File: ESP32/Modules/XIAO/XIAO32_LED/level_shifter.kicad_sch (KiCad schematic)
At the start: 1 part, among them U3 74AHCT125

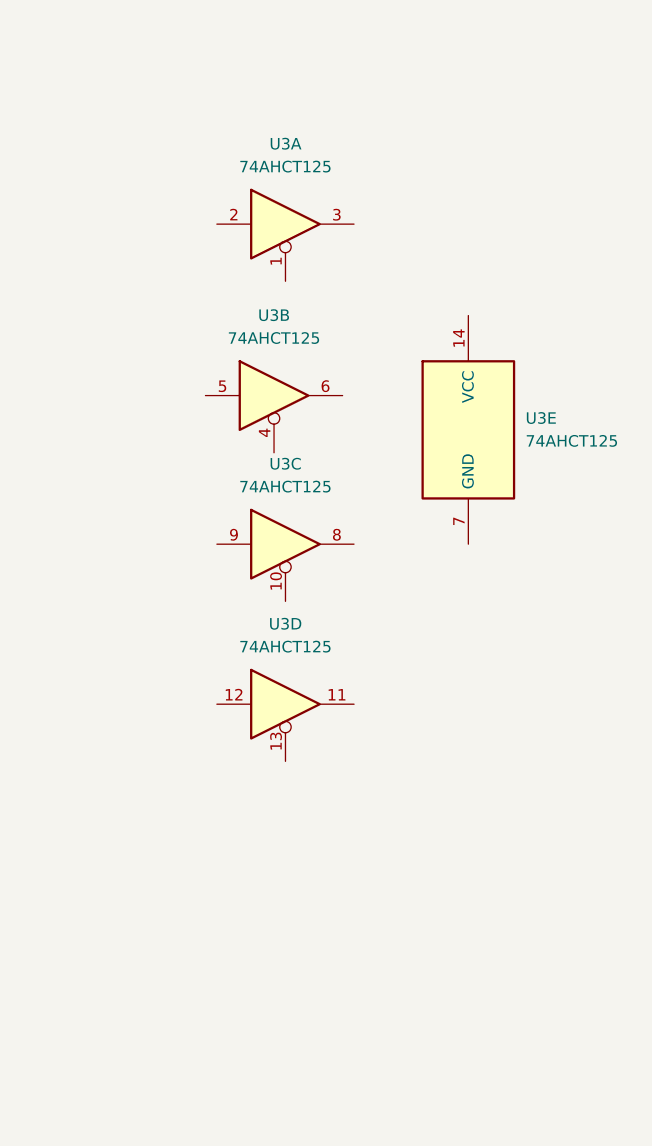
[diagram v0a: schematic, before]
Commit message: XIAO32_LED: MCU wired up
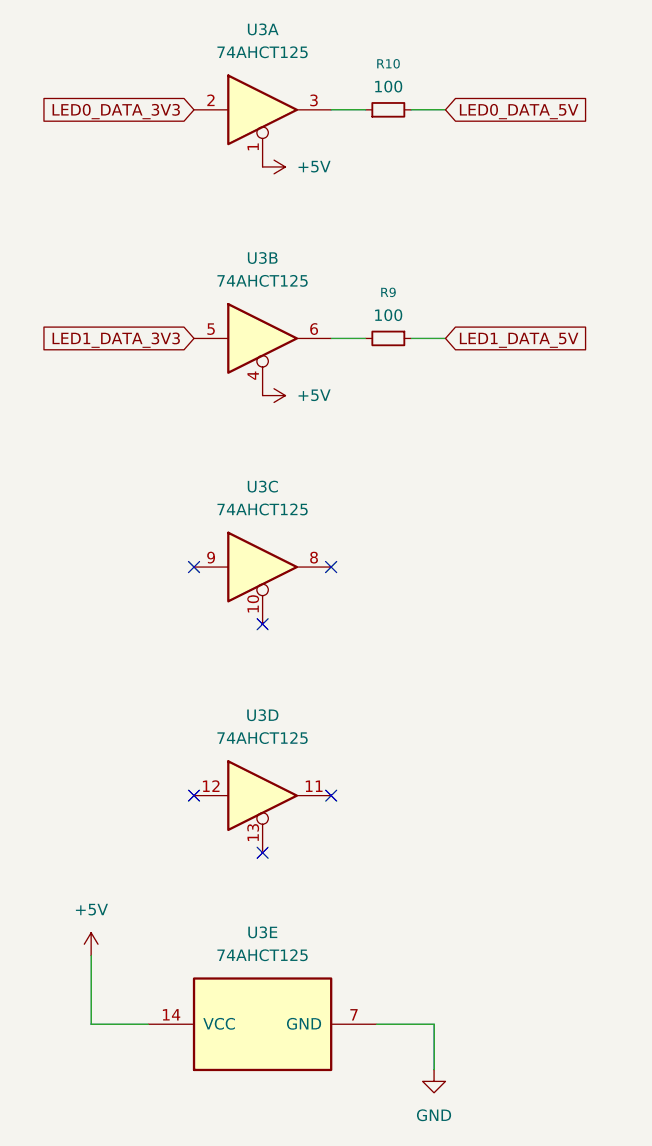
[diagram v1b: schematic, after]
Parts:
- added R10, R9: 100, symbol Device:R_Small
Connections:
- net +5V: now reaches U3.14 (VCC)
- net +5V: now also U3.1, U3.4
- net GND: now reaches U3.7 (GND)
- net LED0_DATA_3V3: now reaches U3.2
- net at U3.3: now also R10.1
- net LED1_DATA_3V3: now reaches U3.5
- net at U3.6: now also R9.2
- new net LED0_DATA_5V: R10.2
- new net LED1_DATA_5V: R9.1
- no-connect marks 0 -> 6
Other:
- moved on the sheet: U3A, U3B, U3C, U3D, U3E
